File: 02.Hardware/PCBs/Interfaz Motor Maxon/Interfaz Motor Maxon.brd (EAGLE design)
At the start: 46 x 44 mm, 4 parts, among them J1 1-84953-1, J2 52207-1133

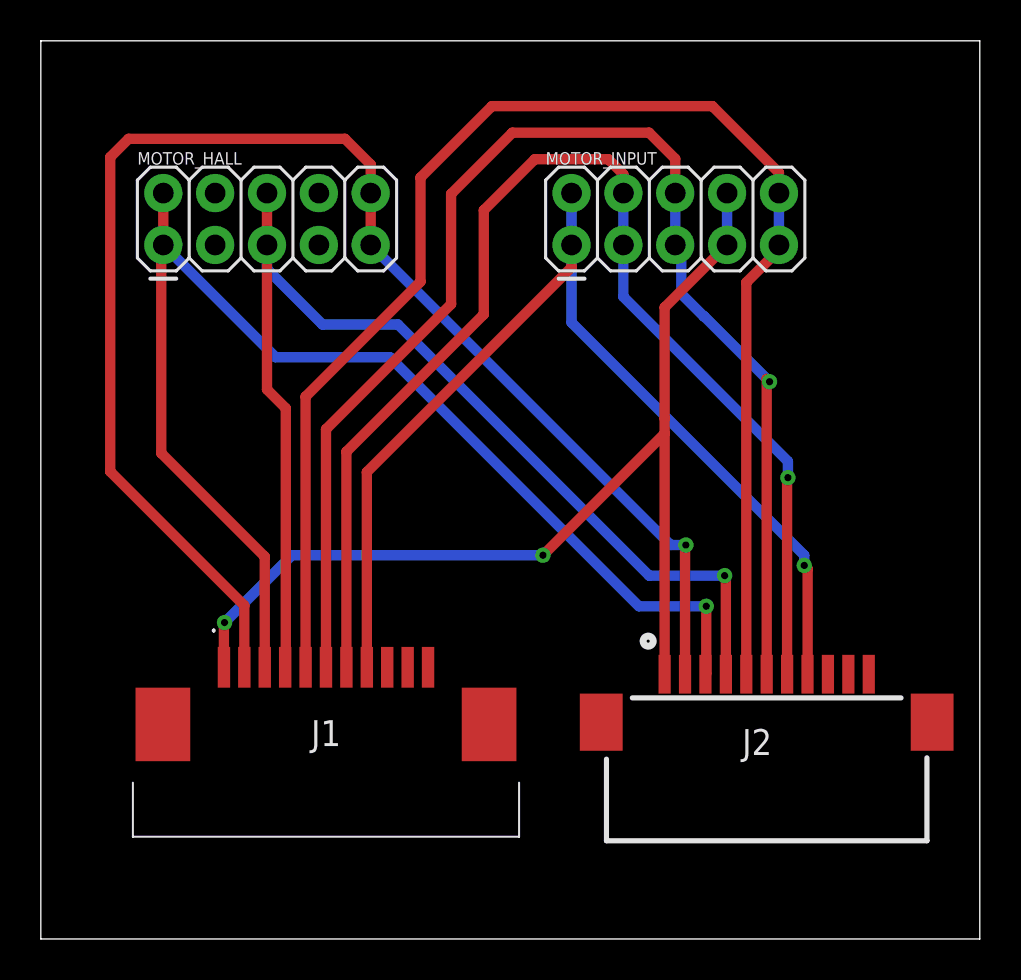
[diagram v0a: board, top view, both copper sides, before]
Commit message: Se genera GERBER para PCBWAY y Cambios menores
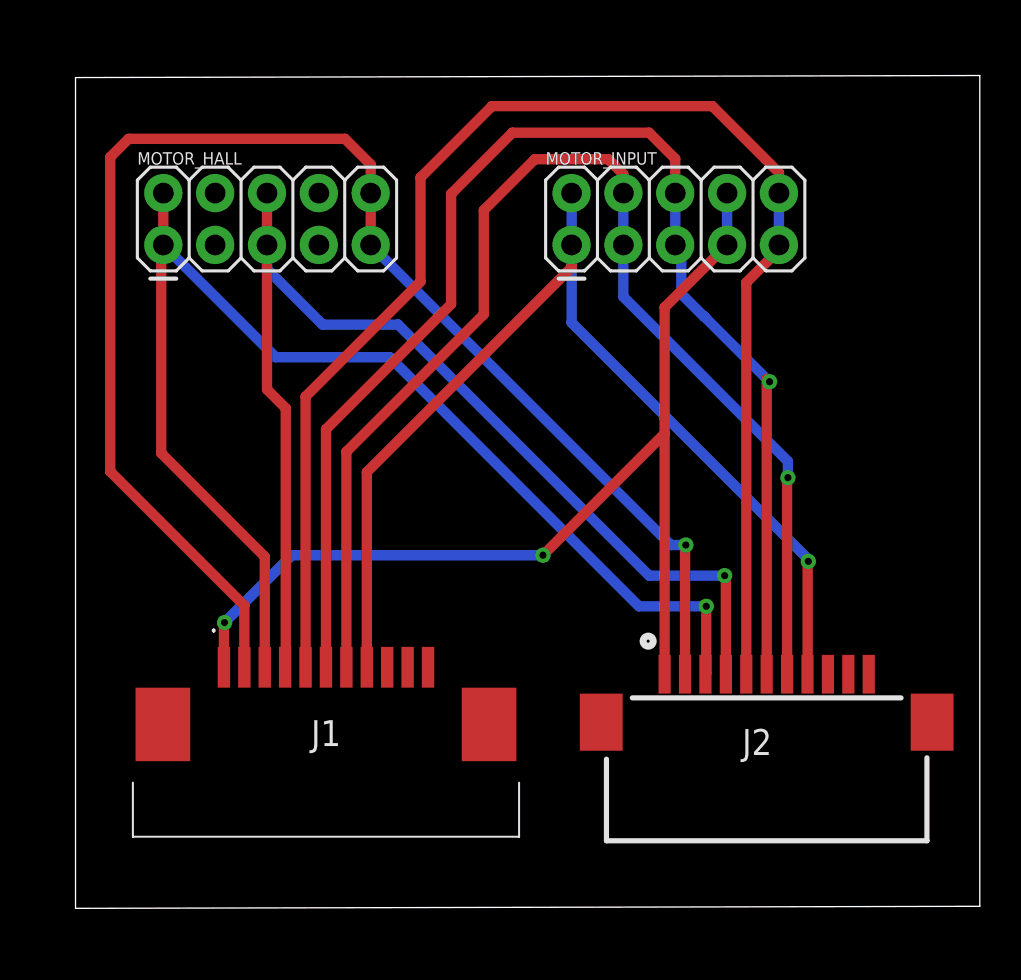
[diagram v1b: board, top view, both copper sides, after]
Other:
- board size 46 x 44 mm -> 44.3 x 40.8 mm
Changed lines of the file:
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@@
 <board>
 <plain>
-<wire x1="0" y1="1" x2="46" y2="1" width="0" layer="20"/>
-<wire x1="46" y1="1" x2="46" y2="45" width="0" layer="20"/>
-<wire x1="46" y1="45" x2="0" y2="45" width="0" layer="20"/>
-<wire x1="0" y1="45" x2="0" y2="1" width="0" layer="20"/>
+<wire x1="1.7" y1="2.5" x2="46" y2="2.6" width="0" layer="20"/>
+<wire x1="46" y1="2.6" x2="46" y2="43.3" width="0" layer="20"/>
+<wire x1="46" y1="43.3" x2="1.7" y2="43.2" width="0" layer="20"/>
+<wire x1="1.7" y1="43.2" x2="1.7" y2="2.5" width="0" layer="20"/>
 <text x="42.8" y="22.9" size="1.778" layer="22" rot="MR0">Interfaz Maxon
 v1-Sep22</text>
@@
 </class>
 </classes>
-<designrules name="default">
+<designrules name="default *">
 <description language="de">&lt;b&gt;EAGLE Design Rules&lt;/b&gt;
 &lt;p&gt;
@@
 <param name="mtCopper" value="0.035mm 0.035mm 0.035mm 0.035mm 0.035mm 0.035mm 0.035mm 0.035mm 0.035mm 0.035mm 0.035mm 0.035mm 0.035mm 0.035mm 0.035mm 0.035mm"/>
 <param name="mtIsolate" value="1.5mm 0.15mm 0.2mm 0.15mm 0.2mm 0.15mm 0.2mm 0.15mm 0.2mm 0.15mm 0.2mm 0.15mm 0.2mm 0.15mm 0.2mm"/>
-<param name="mdWireWire" value="6mil"/>
-<param name="mdWirePad" value="6mil"/>
-<param name="mdWireVia" value="6mil"/>
-<param name="mdPadPad" value="6mil"/>
-<param name="mdPadVia" value="6mil"/>
-<param name="mdViaVia" value="6mil"/>
-<param name="mdSmdPad" value="6mil"/>
-<param name="mdSmdVia" value="6mil"/>
+<param name="mdWireWire" value="12mil"/>
+<param name="mdWirePad" value="12mil"/>
+<param name="mdWireVia" value="12mil"/>
+<param name="mdPadPad" value="12mil"/>
+<param name="mdPadVia" value="12mil"/>
+<param name="mdViaVia" value="12mil"/>
+<param name="mdSmdPad" value="0mil"/>
+<param name="mdSmdVia" value="0mil"/>
 <param name="mdSmdSmd" value="6mil"/>
 <param name="mdViaViaSameLayer" value="6mil"/>
@@
 <contactref element="MOTOR_INPUT" pad="1"/>
 <contactref element="MOTOR_INPUT" pad="2"/>
-<via x="37.4" y="19.3" extent="1-16" drill="0.35"/>
-<wire x1="37.5664" y1="19.1336" x2="37.5664" y2="13.9764" width="0.508" layer="1"/>
+<via x="37.6" y="19.5" extent="1-16" drill="0.35"/>
+<wire x1="37.5664" y1="19.4664" x2="37.5664" y2="13.9764" width="0.508" layer="1"/>
 <wire x1="37.56" y1="13.97" x2="37.5664" y2="13.9764" width="0.508" layer="1"/>
-<wire x1="37.4" y1="19.3" x2="37.5664" y2="19.1336" width="0.508" layer="1"/>
-<wire x1="37.4" y1="19.3" x2="37.4" y2="19.8" width="0.508" layer="16"/>
-<wire x1="37.4" y1="19.8" x2="26" y2="31.2" width="0.508" layer="16"/>
+<wire x1="37.6" y1="19.5" x2="37.5664" y2="19.4664" width="0.508" layer="1"/>
+<wire x1="37.6" y1="19.5" x2="37.6" y2="19.6" width="0.508" layer="16"/>
+<wire x1="37.6" y1="19.6" x2="26" y2="31.2" width="0.508" layer="16"/>
 <wire x1="26" y1="31.2" x2="26" y2="35" width="0.508" layer="16"/>
 <wire x1="26" y1="37.54" x2="26" y2="35" width="0.508" layer="16"/>
